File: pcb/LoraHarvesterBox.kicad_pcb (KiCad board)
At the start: 4 copper layers, 48 x 45.5 mm, 42 parts, among them J1 Conn_01x02_Pin, J2 Conn_01x02_Pin, J3 Conn_01x02_Pin, J4 Conn_01x04_Socket, J5 Conn_01x04_Socket, J6 Conn_01x04_Socket, J7 Conn_01x04_Socket, J8 Conn_01x06_Socket, SW1 SSSS811101, SW2 TS-1088-AR02016, U1 BQ25570, U2 RAK3172-8-SM-I, U3 FM24V10-GTR_C466851

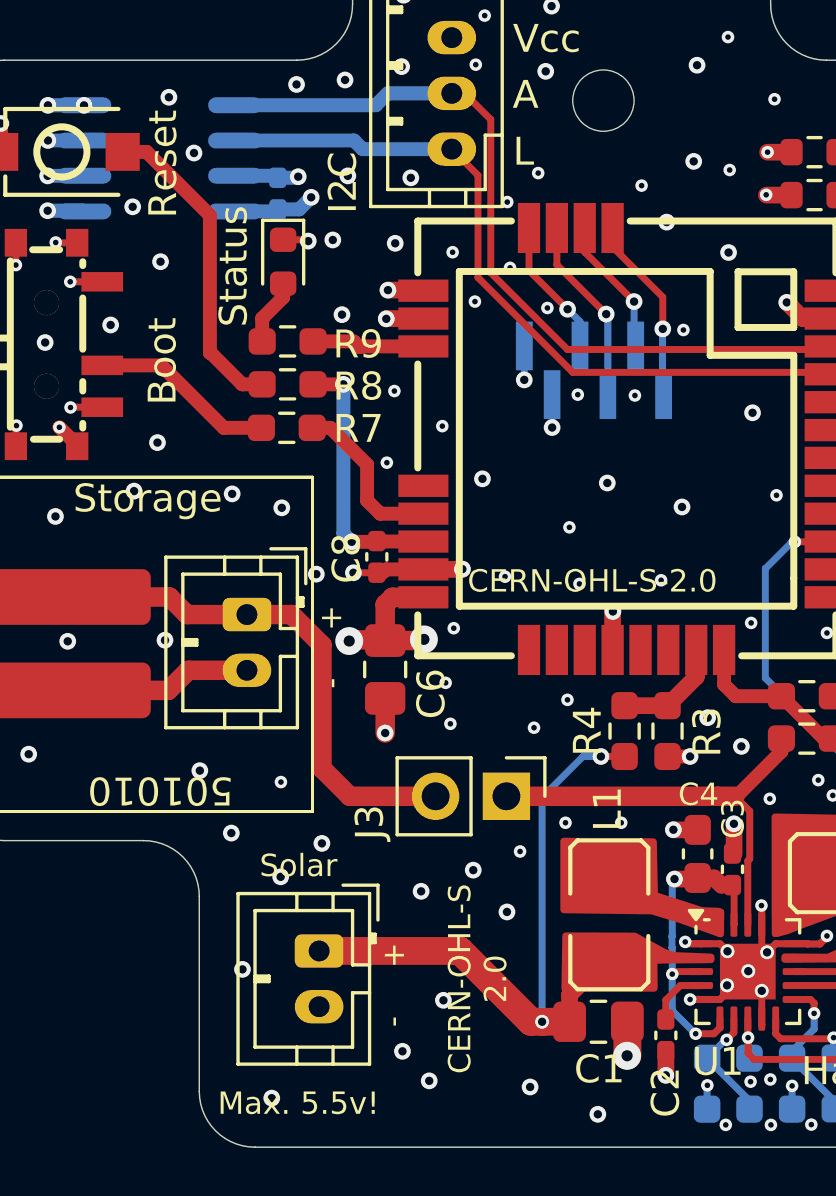
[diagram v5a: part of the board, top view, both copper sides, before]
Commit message: pch, sch: use 0805 capacitor for FRAM and not 0402
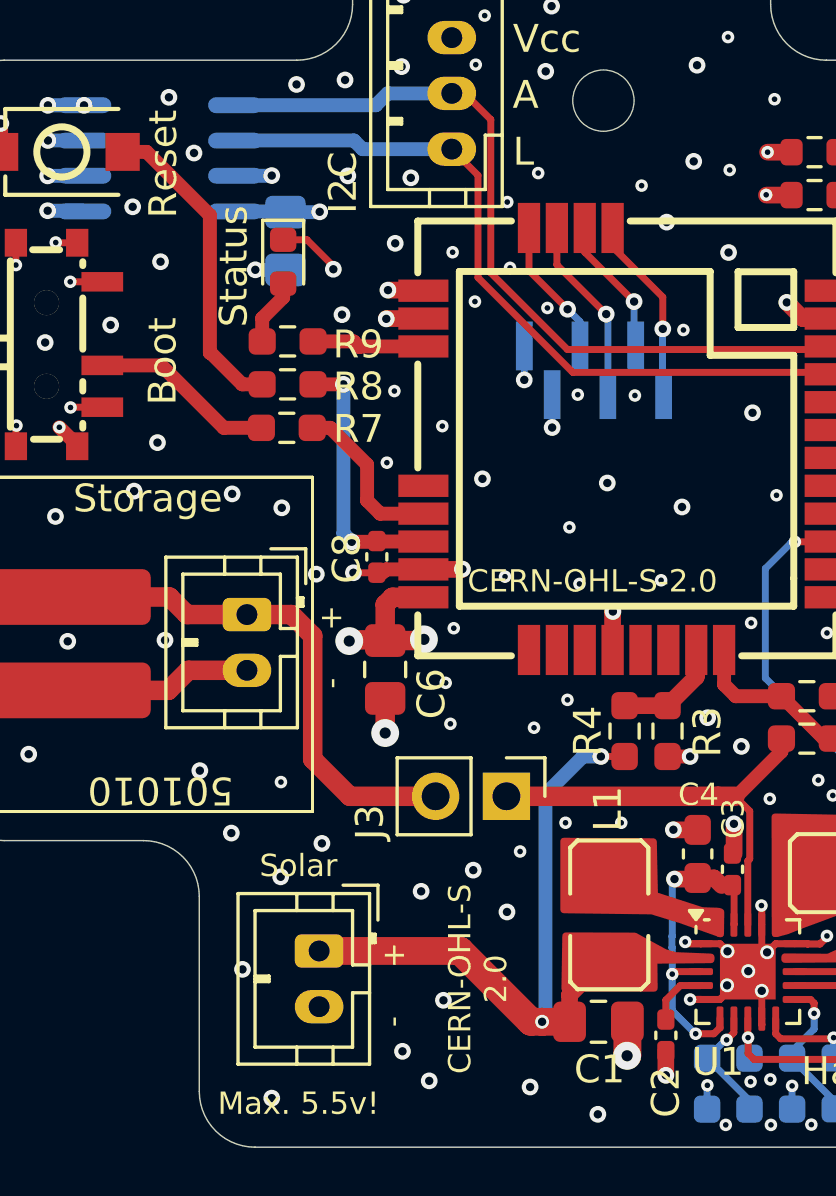
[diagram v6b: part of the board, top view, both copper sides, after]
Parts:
- C7: footprint Capacitor_SMD:C_0402_1005Metric_Pad0.74x0.62mm_HandSolder -> Capacitor_SMD:C_0805_2012Metric_Pad1.18x1.45mm_HandSolder
- moved C7 1.73 mm to (113.1, 67.5), turned to 90 degrees
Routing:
- net GND: track 53.3 -> 54.7 mm

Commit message: pcb: eye candy changes
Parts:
- moved J3 1.06 mm to (120.0, 87.4)
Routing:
- net /VBAT: track 15.8 -> 16.9 mm
- net Net-(BT1-+): track 18.8 -> 17.7 mm
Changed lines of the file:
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@@
 	(footprint "Connector_PinHeader_2.54mm:PinHeader_1x02_P2.54mm_Vertical"
 		(layer "F.Cu")
-		(at 121.02 87.41 -90)
+		(at 119.96 87.36 -90)
 		(descr "Through hole straight pin header, 1x02, 2.54mm pitch, single row")
 		(tags "Through hole pin header THT 1x02 2.54mm single row")
@@
 	)
 	(segment
+		(start 119.96 87.36)
+		(end 120.01 87.41)
+		(width 0.7)
+		(layer "F.Cu")
+		(net 1)
+	)
+	(segment
 		(start 130.8875 85.34)
 		(end 130.8875 85.8025)
@@
 	)
 	(segment
-		(start 128.61 87.41)
-		(end 129.22 87.41)
-		(width 0.7)
-		(layer "F.Cu")
-		(net 1)
-	)
-	(segment
 		(start 129.68125 92.0125)
 		(end 129.68125 89.727626)
@@
 	)
 	(segment
-		(start 121.02 87.41)
-		(end 128.61 87.41)
+		(start 120.01 87.41)
+		(end 129.22 87.41)
 		(width 0.7)
 		(layer "F.Cu")
@@
 	)
 	(segment
-		(start 118.48 87.41)
-		(end 115.4 87.41)
+		(start 109.56 80.89)
+		(end 111.71 80.89)
 		(width 0.7)
 		(layer "F.Cu")
@@
 	)
 	(segment
-		(start 109.56 80.89)
-		(end 111.71 80.89)
+		(start 114.07 81.65)
+		(end 113.31 80.89)
 		(width 0.7)
 		(layer "F.Cu")
@@
 	)
 	(segment
-		(start 114.07 86.08)
-		(end 114.07 81.65)
+		(start 117.42 87.36)
+		(end 117.37 87.41)
 		(width 0.7)
 		(layer "F.Cu")
@@
 	)
 	(segment
-		(start 114.07 81.65)
-		(end 113.31 80.89)
+		(start 117.37 87.41)
+		(end 115.4 87.41)
+		(width 0.7)
+		(layer "F.Cu")
+		(net 15)
+	)
+	(segment
+		(start 114.07 86.08)
+		(end 114.07 81.65)
 		(width 0.7)
 		(layer "F.Cu")

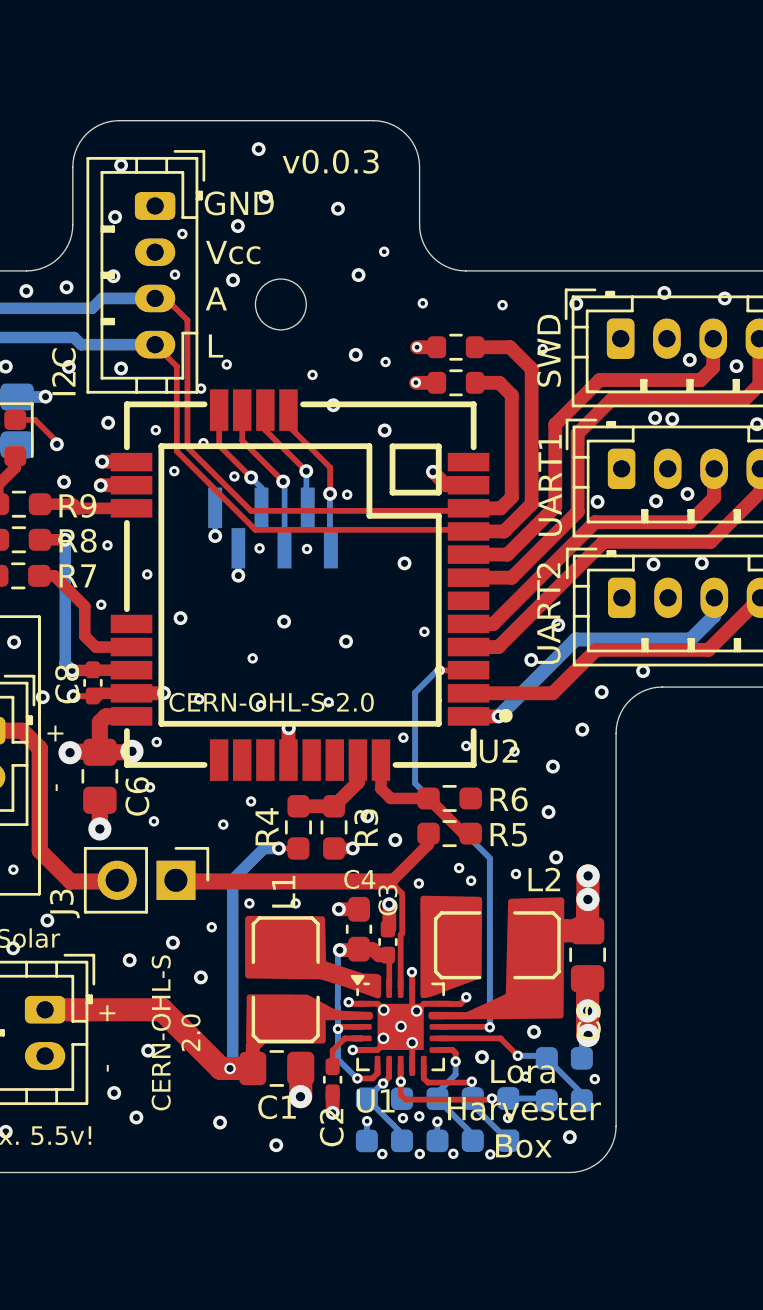
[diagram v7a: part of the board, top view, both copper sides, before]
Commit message: pcb: re-align voltage dividers a bit
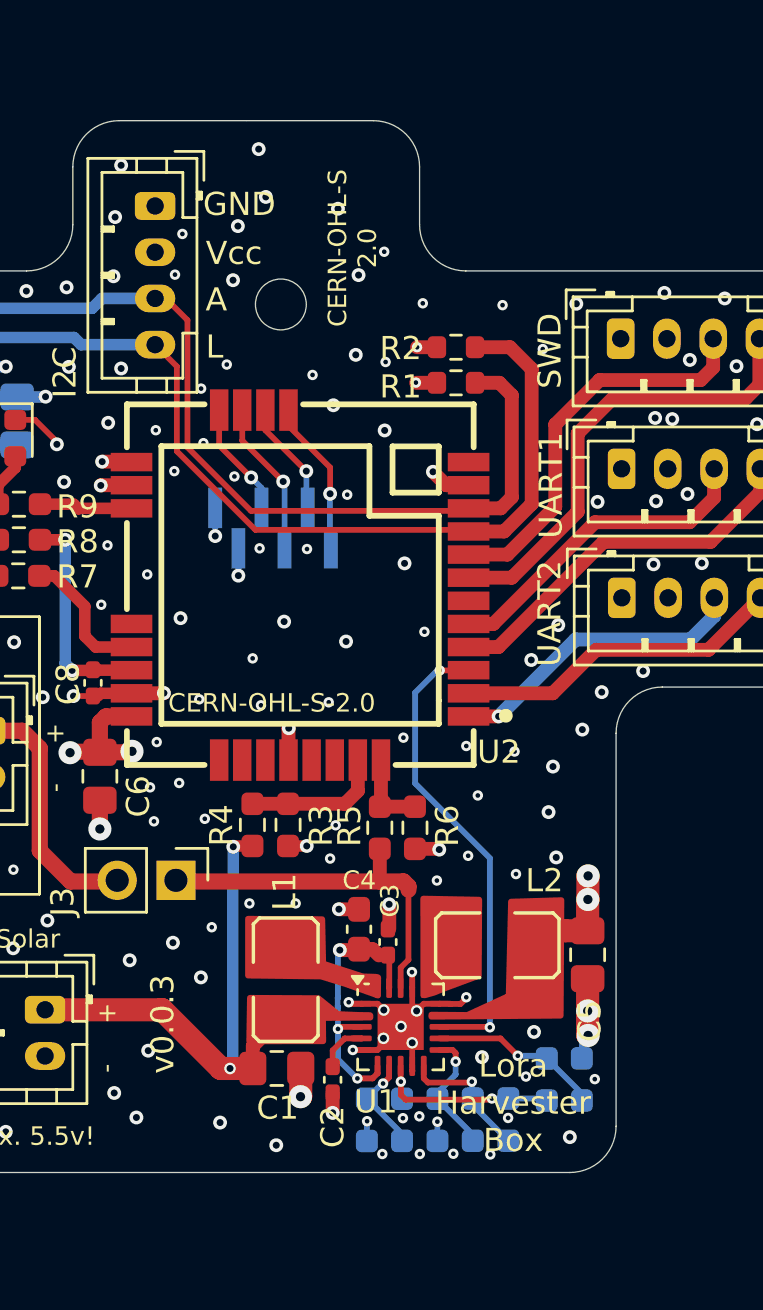
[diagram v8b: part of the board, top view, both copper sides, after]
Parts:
- moved R5 3.03 mm to (128.8, 85.1), turned to 90 degrees
- moved R4 1.99 mm to (123.3, 85.0)
- moved R3 1.99 mm to (124.8, 85.0)
- moved R6 1.96 mm to (130.3, 85.1), turned to -90 degrees
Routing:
- net /ADC_BAT: track 5.93 -> 3.56 mm
- net /ADC_SOL: track 3.96 -> 6.12 mm
- net /VSOLAR: track 26.8 -> 25.7 mm
- net GND: track 54.7 -> 55.7 mm, vias 179 -> 180
- net /VBAT: track 16.9 -> 16.1 mm
